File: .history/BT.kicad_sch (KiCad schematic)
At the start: 94 parts, among them J1 Conn_01x05_Pin, J2 Conn_01x03_Pin, J3 S6B-PH-K-S, J4 Boxed_Header_02x03_SMT, K1 AGQ200S12Z, Q1 BSS123, U1 PCM5100A, U2 ESP32-WROOM-32U, U3 TLV4888DR, U4 TLVM23615RDNR, U5 TLVM23615RDNR, U6 RAA214220, Y1 XO32

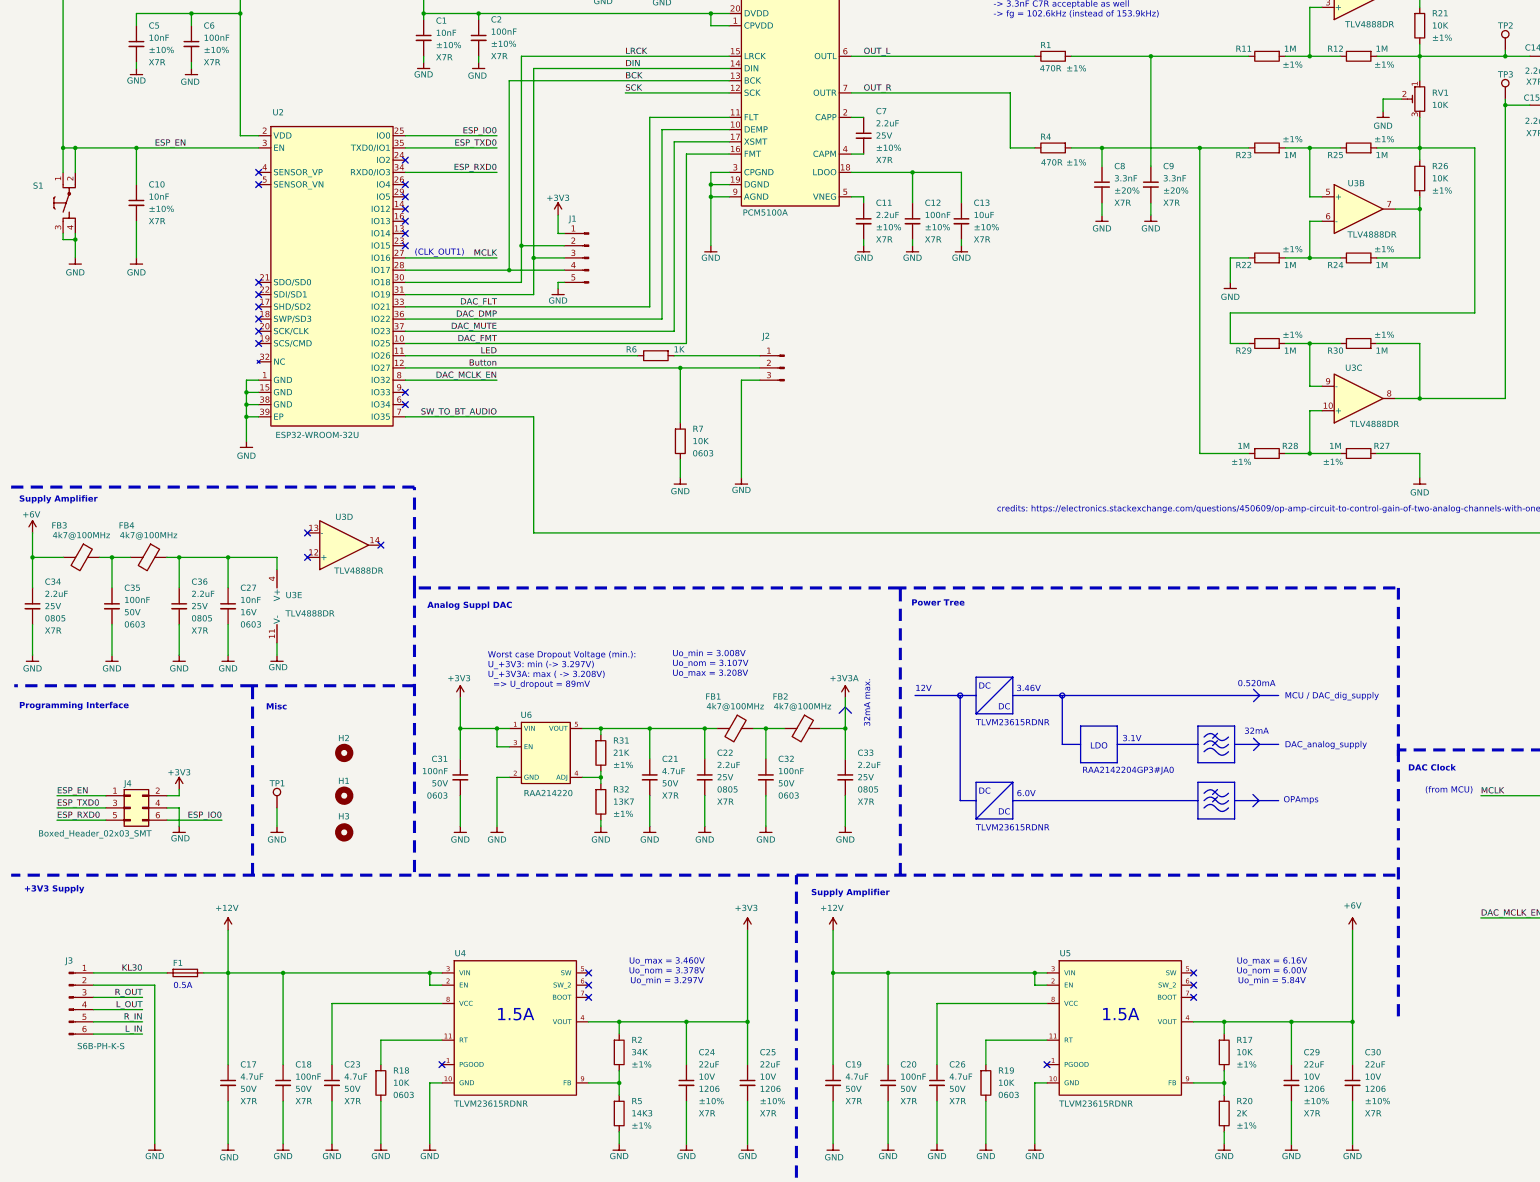
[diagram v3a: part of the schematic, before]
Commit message: rough placement PSU
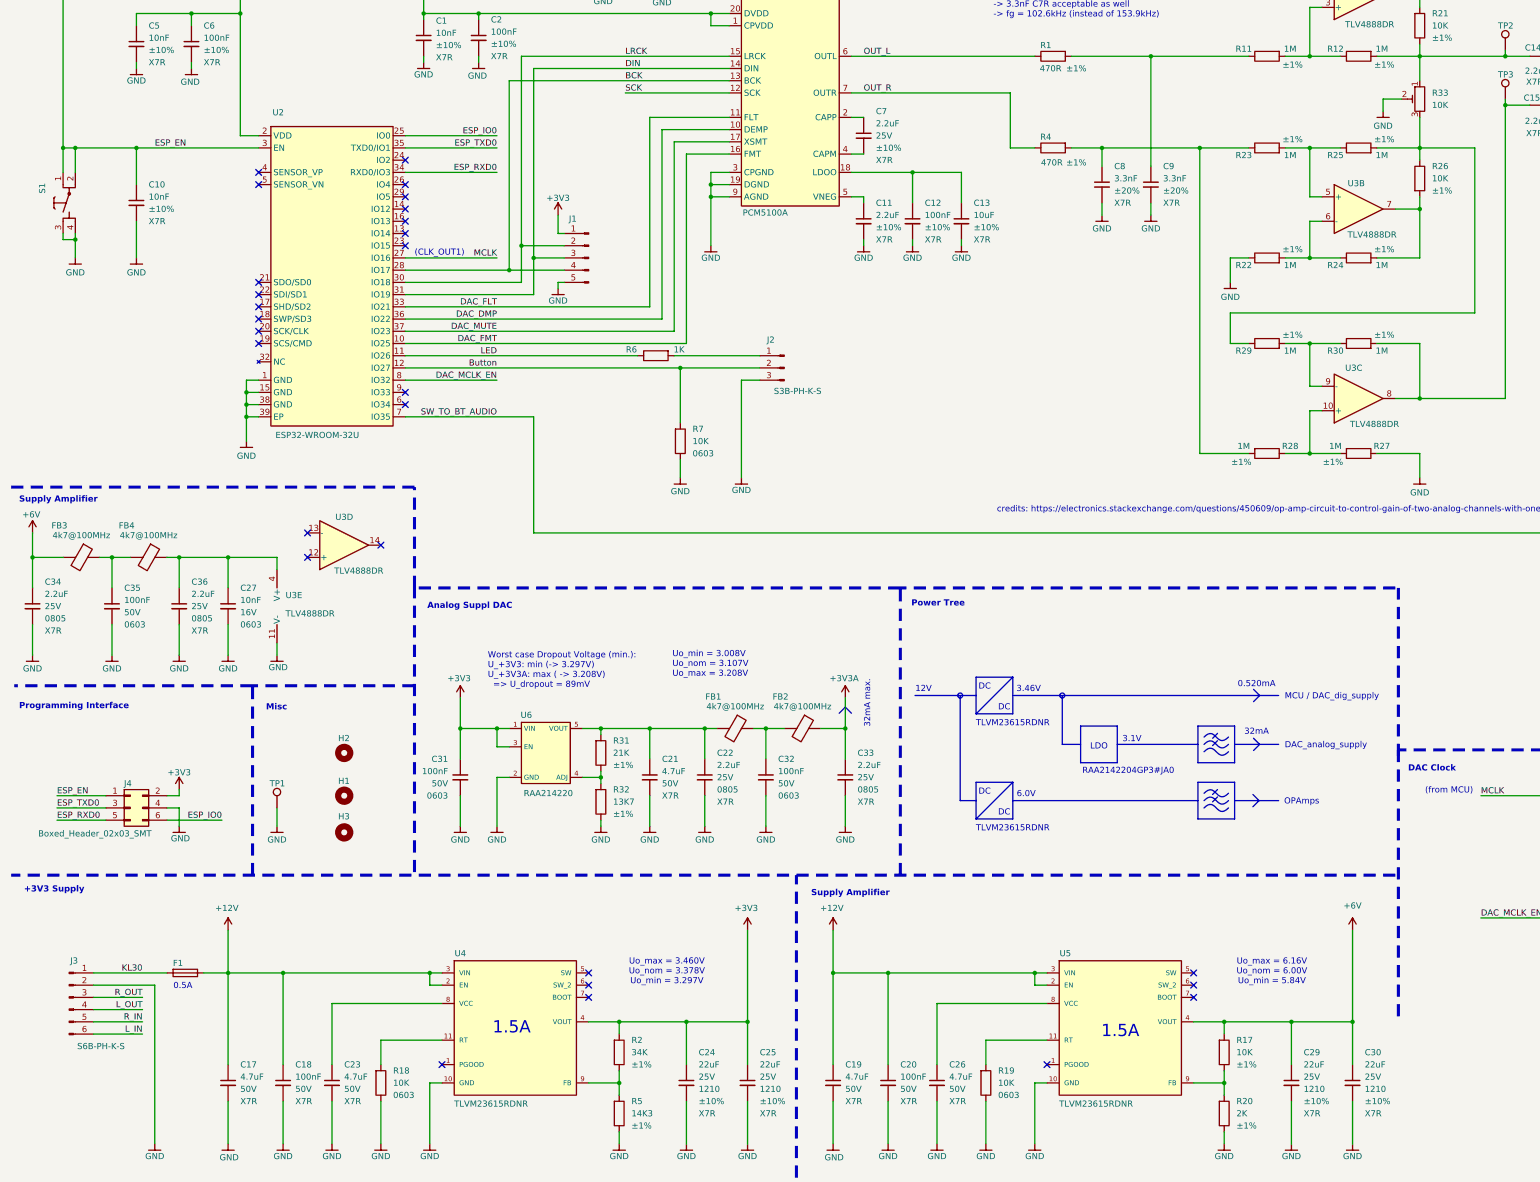
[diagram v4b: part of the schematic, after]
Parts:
- C24, C25, C29, C30: footprint NRD_CAP:C_1206 -> NRD_CAP:C_1210; symbol NRD_C_1206:CL31B226KPHNNNE -> NRD_C_1210:CL32B105KAFNNNE; Manufacturer Part Number CL31B226KPHNNNE -> CL32B105KAFNNNE; Package 1206 -> 1210; Voltage 10V -> 25V; Voltage [V] 10 -> 25
- J2: value Conn_01x03_Pin -> S3B-PH-K-S; footprint (none) -> NRD_CON:S3B-PH-K-S; symbol Connector:Conn_01x03_Pin -> NRD_CON:S3B-PH-K-S; Manufacturer (none) -> JST; Manufacturer Part Number (none) -> S3B-PH-K-S; Maximum Operating Temperature [°C] (none) -> 85; Minimum Operating Temperature [°C] (none) -> -25; RoHS (none) -> Yes
- R33: renamed from RV1; footprint Potentiometer_SMD:Potentiometer_Bourns_TC33X_Vertical -> NRD_R_Var:TC33X-2; symbol Device:R_Potentiometer_Trim -> NRD_R_Var:TC33X-2-103E; Value [Ohm] (none) -> 10e+03
- S1: value (none) -> 434123025826
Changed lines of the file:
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@@
 	(text "1.5A"
 		(exclude_from_sim no)
-		(at 242.57 251.46 0)
+		(at 242.57 254.762 0)
 		(effects
 			(font
@@
 	(text "OPAmps"
 		(exclude_from_sim no)
-		(at 276.479 206.756 0)
+		(at 276.606 207.01 0)
 		(effects
 			(font
@@
 	(text "1.5A"
 		(exclude_from_sim no)
-		(at 116.84 251.46 0)
+		(at 116.078 254 0)
 		(effects
 			(font
@@
 		(dnp no)
 		(property "Reference" "S1"
-			(at 18.796 78.994 90)
+			(at 18.542 79.502 0)
 			(show_name no)
 			(do_not_autoplace no)
@@
 					(size 1.27 1.27)
 				)
-				(justify left)
 			)
 		)
-		(property "Value" ""
-			(at 24.13 82.55 0)
+		(property "Value" "434123025826"
+			(at 21.844 93.472 90)
+			(hide yes)
 			(show_name no)
 			(do_not_autoplace no)
@@
 	)
 	(symbol
-		(lib_id "NRD_C_1206:CL31B226KPHNNNE")
+		(lib_id "NRD_C_1210:CL32B105KAFNNNE")
 		(at 152.4 265.43 0)
 		(unit 1)
@@
 			)
 		)
-		(property "Footprint" "NRD_CAP:C_1206"
+		(property "Footprint" "NRD_CAP:C_1210"
 			(at 152.654 279.908 0)
 			(hide yes)
@@
 			)
 		)
-		(property "Description" "CAP 22uF ±10% 10V X7R 1206"
+		(property "Description" "CAP 22uF ±10% 25V X7R 1210"
 			(at 152.654 279.908 0)
 			(hide yes)
@@
 			)
 		)
-		(property "Manufacturer Part Number" "CL31B226KPHNNNE"
+		(property "Manufacturer Part Number" "CL32B105KAFNNNE"
 			(at 152.654 279.908 0)
 			(hide yes)
@@
 			)
 		)
-		(property "Voltage" "10V"
+		(property "Voltage" "25V"
 			(at 154.94 264.1662 0)
 			(show_name no)
@@
 			)
 		)
-		(property "Voltage [V]" "10"
+		(property "Voltage [V]" "25"
 			(at 147.32 282.194 0)
 			(hide yes)
@@
 			)
 		)
-		(property "Package" "1206"
+		(property "Package" "1210"
 			(at 154.94 266.7062 0)
 			(show_name no)
@@
 	)
 	(symbol
-		(lib_id "Device:R_Potentiometer_Trim")
+		(lib_id "NRD_R_Var:TC33X-2-103E")
 		(at 304.8 60.96 0)
 		(mirror y)
@@
 		(in_pos_files yes)
 		(dnp no)
-		(property "Reference" "RV1"
+		(property "Reference" "R33"
 			(at 307.34 59.6899 0)
 			(show_name no)
@@
 			)
 		)
-		(property "Footprint" "Potentiometer_SMD:Potentiometer_Bourns_TC33X_Vertical"
-			(at 304.8 60.96 0)
-			(hide yes)
-			(show_name no)
-			(do_not_autoplace no)
-			(effects
-				(font
-					(size 1.27 1.27)
-				)
-			)
-		)
-		(property "Datasheet" ""
-			(at 304.8 60.96 0)
-			(hide yes)
-			(show_name no)
-			(do_not_autoplace no)
-			(effects
-				(font
-					(size 1.27 1.27)
-				)
-			)
-		)
-		(property "Description" "Trim-potentiometer"
+		(property "Footprint" "NRD_R_Var:TC33X-2"
 			(at 304.8 60.96 0)
 			(hide yes)
@@
 			)
 		)
-		(property "Sim.Device" "R"
+		(property "Datasheet" "${NERDTRONIX_COMPONENTS_DIR}/Ds/TC33.pdf"
 			(at 304.8 60.96 0)
 			(hide yes)
@@
 			)
 		)
-		(property "Sim.Type" "POT"
+		(property "Description" "Trimme 10k SMT"
 			(at 304.8 60.96 0)
 			(hide yes)
@@
 			)
 		)
-		(property "Sim.Pins" "1=r0 2=wiper 3=r1"
+		(property "Value [Ohm]" "10e+03"
 			(at 304.8 60.96 0)
 			(hide yes)
@@
 			(project "BT"
 				(path "/2a39086a-f2b2-4072-a3e4-22a9fe5f90b0"
-					(reference "RV1")
+					(reference "R33")
 					(unit 1)
 				)
@@
 	)
 	(symbol
-		(lib_id "NRD_C_1206:CL31B226KPHNNNE")
+		(lib_id "NRD_C_1210:CL32B105KAFNNNE")
 		(at 278.13 265.43 0)
 		(unit 1)
@@
 			)
 		)
-		(property "Footprint" "NRD_CAP:C_1206"
+		(property "Footprint" "NRD_CAP:C_1210"
 			(at 278.384 279.908 0)
 			(hide yes)
@@
 			)
 		)
-		(property "Description" "CAP 22uF ±10% 10V X7R 1206"
+		(property "Description" "CAP 22uF ±10% 25V X7R 1210"
 			(at 278.384 279.908 0)
 			(hide yes)
@@
 			)
 		)
-		(property "Manufacturer Part Number" "CL31B226KPHNNNE"
+		(property "Manufacturer Part Number" "CL32B105KAFNNNE"
 			(at 278.384 279.908 0)
 			(hide yes)
@@
 			)
 		)
-		(property "Voltage" "10V"
+		(property "Voltage" "25V"
 			(at 280.67 264.1662 0)
 			(show_name no)
@@
 			)
 		)
-		(property "Voltage [V]" "10"
+		(property "Voltage [V]" "25"
 			(at 273.05 282.194 0)
 			(hide yes)
@@
 			)
 		)
-		(property "Package" "1206"
+		(property "Package" "1210"
 			(at 280.67 266.7062 0)
 			(show_name no)
@@
 	)
 	(symbol
-		(lib_id "NRD_C_1206:CL31B226KPHNNNE")
+		(lib_id "NRD_C_1210:CL32B105KAFNNNE")
 		(at 290.83 265.43 0)
 		(unit 1)
@@
 			)
 		)
-		(property "Footprint" "NRD_CAP:C_1206"
+		(property "Footprint" "NRD_CAP:C_1210"
 			(at 291.084 279.908 0)
 			(hide yes)
@@
 			)
 		)
-		(property "Description" "CAP 22uF ±10% 10V X7R 1206"
+		(property "Description" "CAP 22uF ±10% 25V X7R 1210"
 			(at 291.084 279.908 0)
 			(hide yes)
@@
 			)
 		)
-		(property "Manufacturer Part Number" "CL31B226KPHNNNE"
+		(property "Manufacturer Part Number" "CL32B105KAFNNNE"
 			(at 291.084 279.908 0)
 			(hide yes)
@@
 			)
 		)
-		(property "Voltage" "10V"
+		(property "Voltage" "25V"
 			(at 293.37 264.1662 0)
 			(show_name no)
@@
 			)
 		)
-		(property "Voltage [V]" "10"
+		(property "Voltage [V]" "25"
 			(at 285.75 282.194 0)
 			(hide yes)
@@
 			)
 		)
-		(property "Package" "1206"
+		(property "Package" "1210"
 			(at 293.37 266.7062 0)
 			(show_name no)
@@
 	)
 	(symbol
-		(lib_id "NRD_C_1206:CL31B226KPHNNNE")
+		(lib_id "NRD_C_1210:CL32B105KAFNNNE")
 		(at 165.1 265.43 0)
 		(unit 1)
@@
 			)
 		)
-		(property "Footprint" "NRD_CAP:C_1206"
+		(property "Footprint" "NRD_CAP:C_1210"
 			(at 165.354 279.908 0)
 			(hide yes)
@@
 			)
 		)
-		(property "Description" "CAP 22uF ±10% 10V X7R 1206"
+		(property "Description" "CAP 22uF ±10% 25V X7R 1210"
 			(at 165.354 279.908 0)
 			(hide yes)
@@
 			)
 		)
-		(property "Manufacturer Part Number" "CL31B226KPHNNNE"
+		(property "Manufacturer Part Number" "CL32B105KAFNNNE"
 			(at 165.354 279.908 0)
 			(hide yes)
@@
 			)
 		)
-		(property "Voltage" "10V"
+		(property "Voltage" "25V"
 			(at 167.64 264.1662 0)
 			(show_name no)
@@
 			)
 		)
-		(property "Voltage [V]" "10"
+		(property "Voltage [V]" "25"
 			(at 160.02 282.194 0)
 			(hide yes)
@@
 			)
 		)
-		(property "Package" "1206"
+		(property "Package" "1210"
 			(at 167.64 266.7062 0)
 			(show_name no)
@@
 		(dnp no)
 		(property "Reference" "J3"
-			(at 24.13 240.03 0)
+			(at 25.146 240.03 0)
 			(show_name no)
 			(do_not_autoplace no)
@@
 	)
 	(symbol
-		(lib_id "Connector:Conn_01x03_Pin")
-		(at 172.72 116.84 0)
+		(lib_id "NRD_CON:S3B-PH-K-S")
+		(at 168.91 116.84 0)
 		(mirror y)
 		(unit 1)
@@
 		(dnp no)
 		(property "Reference" "J2"
-			(at 168.148 110.236 0)
+			(at 169.926 110.998 0)
+			(show_name no)
+			(do_not_autoplace no)
+			(effects
+				(font
+					(size 1.27 1.27)
+				)
+			)
+		)
+		(property "Value" "S3B-PH-K-S"
+			(at 175.514 121.666 0)
 			(show_name no)
 			(do_not_autoplace no)
@@
 					(size 1.27 1.27)
 				)
-				(justify right)
 			)
 		)
-		(property "Value" "Conn_01x03_Pin"
-			(at 173.99 118.1099 0)
+		(property "Footprint" "NRD_CON:S3B-PH-K-S"
+			(at 168.91 116.84 0)
 			(hide yes)
 			(show_name no)
@@
 					(size 1.27 1.27)
 				)
-				(justify right)
 			)
 		)
-		(property "Footprint" ""
-			(at 172.72 116.84 0)
+		(property "Datasheet" "${NERDTRONIX_COMPONENTS_DIR}/Ds/JST_PH_Series.pdf"
+			(at 168.91 116.84 0)
 			(hide yes)
 			(show_name no)
@@
 			)
 		)
-		(property "Datasheet" ""
-			(at 172.72 116.84 0)
+		(property "Description" "JST PH Series 01x03 Angled THT"
+			(at 168.91 116.84 0)
+			(hide yes)
+			(show_name no)
+			(do_not_autoplace no)
+			(effects
+				(font
+					(size 1.27 1.27)
+				)
+			)
+		)
+		(property "Minimum Operating Temperature [°C]" "-25"
+			(at 168.91 116.84 0)
+			(hide yes)
+			(show_name no)
+			(do_not_autoplace no)
+			(effects
+				(font
+					(size 1.27 1.27)
+				)
+			)
+		)
+		(property "Maximum Operating Temperature [°C]" "85"
+			(at 168.91 116.84 0)
+			(hide yes)
+			(show_name no)
+			(do_not_autoplace no)
+			(effects
+				(font
+					(size 1.27 1.27)
+				)
+			)
+		)
+		(property "Manufacturer Part Number" "S3B-PH-K-S"
+			(at 168.91 116.84 0)
 			(hide yes)
 			(show_name no)
@@
 			)
 		)
-		(property "Description" "Generic connector, single row, 01x03, script generated"
-			(at 172.72 116.84 0)
+		(property "Manufacturer" "JST"
+			(at 168.91 116.84 0)
+			(hide yes)
+			(show_name no)
+			(do_not_autoplace no)
+			(effects
+				(font
+					(size 1.27 1.27)
+				)
+			)
+		)
+		(property "RoHS" "Yes"
+			(at 168.91 116.84 0)
 			(hide yes)
 			(show_name no)

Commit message: replaced all components by library parts
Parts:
- removed C22, C34: 2.2uF, NRD_CAP:C_0805, symbol NRD_C_0805:CL21B225KAFNNNE
- removed FB1, FB3: 4k7@100MHz, symbol Device:FerriteBead
- removed FB2, FB4: 4k7@100MHz, Inductor_SMD:L_0805_2012Metric, symbol Device:FerriteBead
- removed J1: Conn_01x05_Pin, Connector_PinHeader_2.54mm:PinHeader_1x05_P2.54mm_Vertical, symbol Connector:Conn_01x05_Pin
- added C22: 100nF, NRD_CAP:C_0603, symbol NRD_C_0603:CL10B104KB8NNNC
- added J1: 61300511121, NRD_PinHeader:61300511121, symbol NRD_PinHeader:61300511121
- added L1, L2, L3, L4: 10uH, NRD_IND:74479777310, symbol NRD_IND:74479777310
- added R34: 10K, NRD_RES:R_0603, symbol NRD_R_0603:RC0603FR-0710KL
- added R35: 1K, NRD_RES:R_0603, symbol NRD_R_0603:RC0603FR-071KL
- added TP4, TP5: 5001, NRD_MISC:500x, symbol NRD_MISC:5001
- D1: value D_Schottky -> VSSAF5N50-M3/6B; footprint (none) -> NRD_Diodes:VSSAF5N50; symbol Device:D_Schottky -> NRD_Diodes:VSSAF5N50-M3/6B; Manufacturer (none) -> Visha; Manufacturer Part Number (none) -> VSSAF5N50-M3/6B; Maximum Operating Temperature [°C] (none) -> 150; Minimum Operating Temperature [°C] (none) -> -40; Rated Current (none) -> 5.0A; Rated Current [A] (none) -> 5.0; RoHS (none) -> Yes; Voltage (none) -> 0.56V; Voltage [V] (none) -> 0.56
- F1: value Fuse -> SF-1206S050-2; footprint Fuse:Fuse_0805_2012Metric -> NRD_Fuse:SF-1206S; symbol Device:Fuse -> NRD_Fuse:SF-1206S050-2; Manufacturer (none) -> Bourns; Manufacturer Part Number (none) -> SF-1206S050-2; Maximum Operating Temperature [°C] (none) -> 105; Minimum Operating Temperature [°C] (none) -> -20; Rated Current (none) -> 0.5A; Rated Current [A] (none) -> 0.5; RoHS (none) -> Yes; Voltage (none) -> 63VDC; Voltage [V] (none) -> 63
- K1: value AGQ200S12Z -> AGQ200A12Z; footprint NRD_Relays:AGQ200Sxxx -> NRD_Relays:AGQ200Axxx; symbol NRD_Relays:AGQ200S12Z -> NRD_Relays:AGQ200A12Z; Manufacturer Panasonic Electric Works -> Panasonic; Manufacturer Part Number AGQ200S12Z -> AGQ200A12Z
- M1: renamed from H1; value MountingHole -> Mounting_Hole_2.7mm_Unplated; footprint MountingHole:MountingHole_2.7mm_M2.5_ISO7380 -> NRD_MECH:Mounting_Hole_2.7mm_Unplated; symbol Mechanical:MountingHole -> NRD_MECH:Mounting Hole 2.7mm Unplated
- M2: renamed from H2; value MountingHole -> Mounting_Hole_2.7mm_Unplated; footprint MountingHole:MountingHole_2.7mm_M2.5_ISO7380 -> NRD_MECH:Mounting_Hole_2.7mm_Unplated; symbol Mechanical:MountingHole -> NRD_MECH:Mounting Hole 2.7mm Unplated
- M3: renamed from H3; value MountingHole -> Mounting_Hole_2.7mm_Unplated; footprint MountingHole:MountingHole_2.7mm_M2.5_ISO7380 -> NRD_MECH:Mounting_Hole_2.7mm_Unplated; symbol Mechanical:MountingHole -> NRD_MECH:Mounting Hole 2.7mm Unplated
- TP1: value TestPoint -> 5001; footprint TestPoint:TestPoint_Bridge_Pitch2.0mm_Drill0.7mm -> NRD_MISC:500x; symbol Connector:TestPoint -> NRD_MISC:5001; Manufacturer (none) -> Keystone Electronics; Manufacturer Part Number (none) -> 5001; Maximum Operating Temperature [°C] (none) -> 85; Minimum Operating Temperature [°C] (none) -> -45; Net (none) -> GND; RoHS (none) -> Yes
- TP2: value TestPoint -> 5001; footprint TestPoint:TestPoint_Loop_D2.50mm_Drill1.0mm -> NRD_MISC:500x; symbol Connector:TestPoint -> NRD_MISC:5001; Manufacturer (none) -> Keystone Electronics; Manufacturer Part Number (none) -> 5001; Maximum Operating Temperature [°C] (none) -> 85; Minimum Operating Temperature [°C] (none) -> -45; Net (none) -> OUT_L_AMP; RoHS (none) -> Yes
- TP3: value TestPoint -> 5001; footprint TestPoint:TestPoint_Loop_D2.50mm_Drill1.0mm -> NRD_MISC:500x; symbol Connector:TestPoint -> NRD_MISC:5001; Manufacturer (none) -> Keystone Electronics; Manufacturer Part Number (none) -> 5001; Maximum Operating Temperature [°C] (none) -> 85; Minimum Operating Temperature [°C] (none) -> -45; Net (none) -> OUT_R_AMP; RoHS (none) -> Yes
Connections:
- net +12V: now also D1.K; no longer D1.1 (K)
- net +3V3: now also R7.2, J1.1
- net +3V3A: now also L4.2
- net +6V: now also L1.1
- net BCK: now also J1.4
- net Button: now also C22.1, R35.2; no longer J2.2 (Pin_2)
- net DIN: now also J1.3
- net GND: now also C22.2, J1.5, R34.2; no longer R7.2
- net LRCK: now also J1.2
- net OUT_L: now also TP4.1
- net OUT_R: now also TP5.1
- net at K1.8, Q1.3 (D): now also D1.A; no longer D1.2 (A)
- net at C35.1: now also L1.2, L2.1
- net at C32.1: now also L3.2, L4.1
- net +3V3A_OUT: now reaches C21.1, R31.1, U6.5 (VOUT)
- net +3V3A_OUT: now also L3.1
- net at C27.1, C36.1, U3.4 (V+): now also L2.2
- net +3V3A_FB: now reaches R31.2, R32.1, U6.4 (ADJ)
- net DAC_MUTE renamed DAC_MUTEn
- net DAC_MUTEn: now also R34.1
- new net: J2.2 (Pin_2), R35.1
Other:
- note removed: "0.5A"
- moved on the sheet: C14, C15, C21, C31, F1, J2, Q1, R1, R6, R7, R8, TP2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

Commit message: started layout
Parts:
- removed TP4, TP5: 5001, NRD_MISC:500x, symbol NRD_MISC:5001
- J1: now not fitted
- L1, L2, L3, L4: Manufacturer (none) -> Wurrth Elektronik; Manufacturer Part Number (none) -> 74479777310; Maximum Operating Temperature [°C] (none) -> 85; Minimum Operating Temperature [°C] (none) -> -40; RoHS (none) -> RoHS
- R33: Manufacturer (none) -> Bourns; Manufacturer Part Number (none) -> TC33X-2-103E; Maximum Operating Temperature [°C] (none) -> 100; Minimum Operating Temperature [°C] (none) -> -40; RoHS (none) -> Yes
- U1: Manufacturer (none) -> Texas Instruments; Manufacturer Part Number (none) -> PCM5100A; Maximum Operating Temperature [°C] (none) -> 130; Minimum Operating Temperature [°C] (none) -> -40; RoHS (none) -> Yes
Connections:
- net BCK: now also J1.2, U2.31 (IO19); no longer J1.4, U2.28 (IO17)
- net DIN: now also U2.29 (IO5); no longer U2.31 (IO19)
- net LRCK: now also J1.4, U2.28 (IO17); no longer J1.2, U2.30 (IO18)
- net FB_+3V3: now reaches R2.2, R5.1, U4.9 (FB)
- net BUTTON_CON: now reaches J2.2 (Pin_2), R35.1
- net LED_CON: now reaches J2.1 (Pin_1), R6.1
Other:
- note added: "0.183A"
- note added: "552mA"
- note added: "P=1.87W"
- note added: "P=2.19W"
- note added: "f_SW = 400kHZ"
- note added: "η@552mA = 85%"
- moved on the sheet: C17, C18, C23, C24, C25, C5, C6, F1, J2, J3, R18, R2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
